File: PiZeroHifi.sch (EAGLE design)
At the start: 45 parts, among them CON1 RPI-ZEROPI-ZERO-THRUHOLE, CON3 Audio Out, J1 GROVEGROVE-HORIZONTAL, J2 GROVEGROVE-HORIZONTAL, J3 GROVEGROVE-HORIZONTAL, U1 TXS0102, U2 LSM6DS33, U3 TC1014-3.3V, U4 PCM5101A, U5 PAM8403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

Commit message: Route HifiBoard
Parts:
- removed C1: 1500uF, HappyBrackets:WURTH-CAP
- removed R1: 10K, adafruit:R-US_R0603
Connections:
- removed net N$14: CON3.1, U5.+OUTL-1
- removed net N$15: CON3.2, U5.-OUTL-3
- removed net N$16: CON3.3, U5.-OUT_R-14
- removed net N$17: CON3.4, U5.+OUT_R-16
- removed net N$26: C23.2, R15.2, R16.1, U1.OE
- new net +L: CON3.2, U5.+OUTL-1
- new net +R: CON3.3, U5.+OUT_R-16
- new net -L: CON3.1, U5.-OUTL-3
- new net -R: CON3.4, U5.-OUT_R-14
- net +5V: no longer C1.+
- net ACCEL_INT_1: now also CON1.GPIO27/GEN2, U2.INT1; no longer CON1.GPIO17/GEN0, U2.INT2
- net ACCEL_INT_2: now also CON1.GPIO17/GEN0, U2.INT2; no longer CON1.GPIO27/GEN2, U2.INT1
- net GND: no longer C1.-, R1.1
- net OE: now also C23.2, R15.2, R16.1, U1.OE; no longer CON1.GPIO20, R1.2

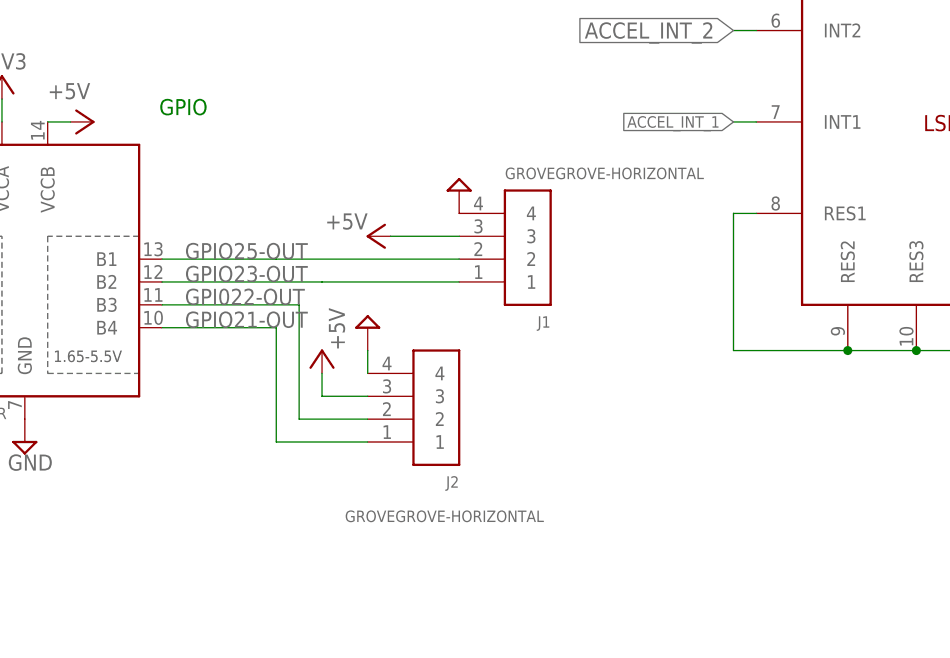
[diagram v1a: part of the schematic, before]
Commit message: Change position of GPIO
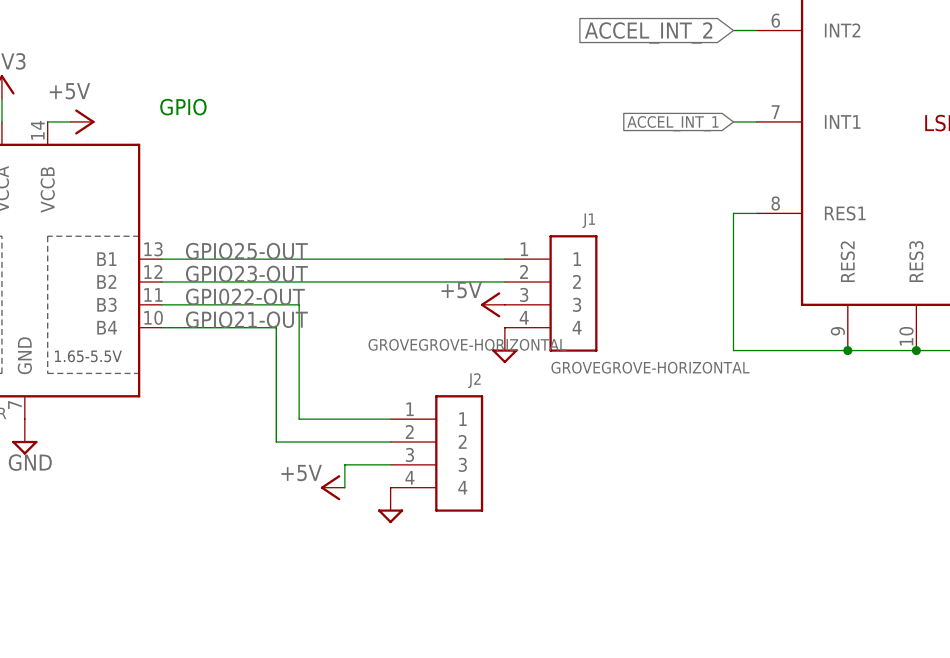
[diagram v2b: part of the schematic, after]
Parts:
- C10, C2: MF (none) -> YAGEO; MPN (none) -> CC0603KRX7R9BB222; OC_FARNELL (none) -> 722194
- C11, C17, C18, C22, C23, C3, C5: MF (none) -> YAGEO; MPN (none) -> CC0603KRX7R7BB104; OC_FARNELL (none) -> 432210
- C12: MF (none) -> AVX; MPN (none) -> 06035C471KAT2A; OC_FARNELL (none) -> 498580
- C13, C14, C15, C7, C9: MF (none) -> AVX; MPN (none) -> 06033C104JAT2A; OC_FARNELL (none) -> 1740614
- C16, C6, C8, CON1, CON3, U1, U2, U4: OC_FARNELL (none) -> unknown
- C19, C20, C21, C4: MF (none) -> AVX; MPN (none) -> 08053D106KAT2A; OC_FARNELL (none) -> 1867958
- R10, R11: MF (none) -> VISHAY; MPN (none) -> CRCW0603470RFKEA; OC_FARNELL (none) -> 1469815
- R12, R13, R15: MF (none) -> YAGEO; MPN (none) -> RC0603FR-0710KL; OC_FARNELL (none) -> 9238603
- R14, R16, R7: MF (none) -> MULTICOMP PRO; MPN (none) -> MCWR06X1001FTL; OC_FARNELL (none) -> 2447272RL
- R8, R9: MF (none) -> PANASONIC; MPN (none) -> ERJ3EKF1433V; OC_FARNELL (none) -> 2303238
- U3: MF (none) -> MICROCHIP; MPN (none) -> TC1014-3.3VCT713; OC_FARNELL (none) -> 1331502
- U5: MF (none) -> DIODES INC.; OC_FARNELL (none) -> 3373823
- U6: MPN TXB0104PWR -> TXB0104PWR .
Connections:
- net GPI022-OUT: now also J2.1; no longer J2.2
- net GPIO21-OUT: now also J2.2; no longer J2.1
- net GPIO23-OUT: now also J1.2; no longer J1.1
- net GPIO25-OUT: now also J1.1; no longer J1.2
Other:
- moved on the sheet: J1, J2
